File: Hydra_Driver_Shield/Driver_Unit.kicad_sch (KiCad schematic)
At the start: 29 parts, among them IC2 DRV8313RHHR, U3 74HC32, U4 INA199xxDCK, U5 INA199xxDCK

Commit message: Finished updating shield board with changes
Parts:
- removed C23: 0.1u, Capacitor_SMD:C_0402_1005Metric, symbol Device:C_Small
- removed R11, R12, R13, R14, R15, R16: 3.3k, Resistor_SMD:R_0402_1005Metric, symbol Device:R
- removed U3: 74HC32, Package_SO:SOIC-14_3.9x8.7mm_P1.27mm, symbol TacTile:74HC32
- renumbered R17 to R10, R18 to R11, R19 to R12, R20 to R13, R21 to R14, R22 to R15, R23 to R16, U4 to U3, U5 to U4
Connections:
- net IN1H renamed IN1
- net IN2H renamed IN2
- net IN3H renamed IN3

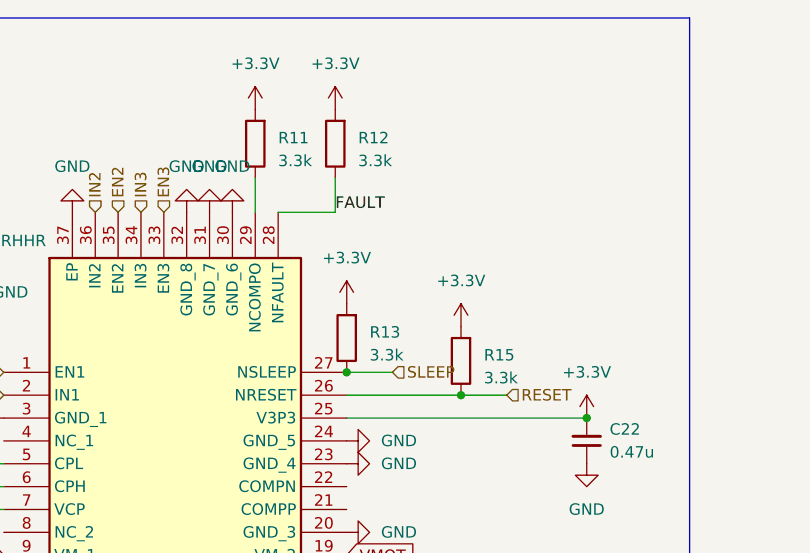
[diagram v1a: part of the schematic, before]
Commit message: Consolidated pullup resistors to 10k
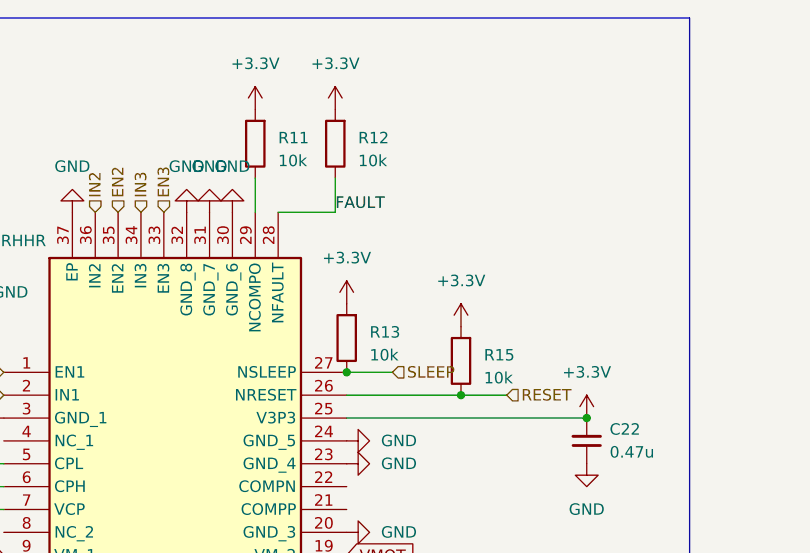
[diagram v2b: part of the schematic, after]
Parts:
- R11, R12, R13, R15: value 3.3k -> 10k
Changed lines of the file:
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@@
 			)
 		)
-		(property "Value" "3.3k"
+		(property "Value" "10k"
 			(at 116.84 48.895 0)
 			(effects
@@
 			)
 		)
-		(property "Value" "3.3k"
+		(property "Value" "10k"
 			(at 106.68 27.305 0)
 			(effects
@@
 			)
 		)
-		(property "Value" "3.3k"
+		(property "Value" "10k"
 			(at 115.57 27.305 0)
 			(effects
@@
 			)
 		)
-		(property "Value" "3.3k"
+		(property "Value" "10k"
 			(at 129.54 51.435 0)
 			(effects
